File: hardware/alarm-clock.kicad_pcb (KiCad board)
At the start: 2 copper layers, 95.3 x 86.4 mm, 37 parts, among them CON1 BARREL_JACK, CON2 BARREL_JACK, IC1 ATMEGA328-P, Q1 Q_NPN_BCE, SW1 SWITCH_INV, SW2 SW_PUSH, SW3 SW_PUSH, U1 LM7805CT, U2 DS1307, U3 4Dig7Seg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

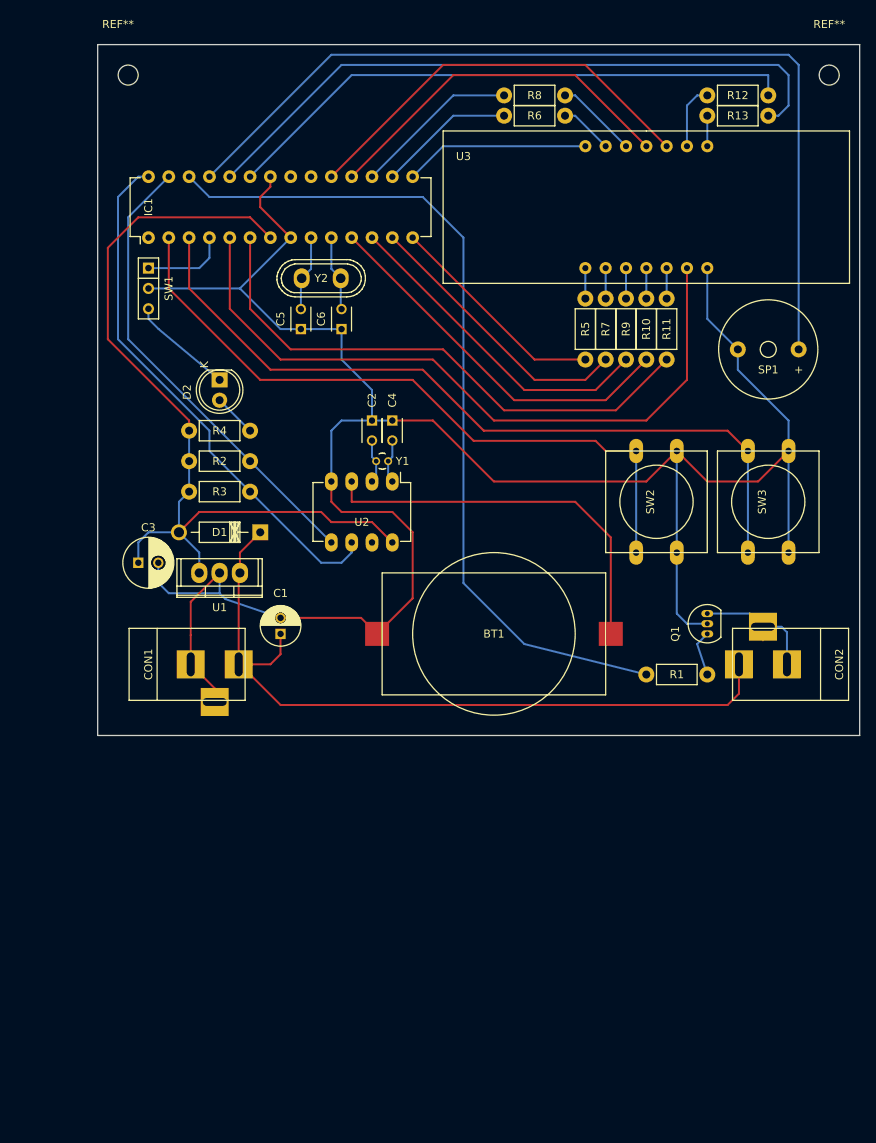
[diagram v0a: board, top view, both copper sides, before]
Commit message: Updated schematic w/ SMD and working buzzer
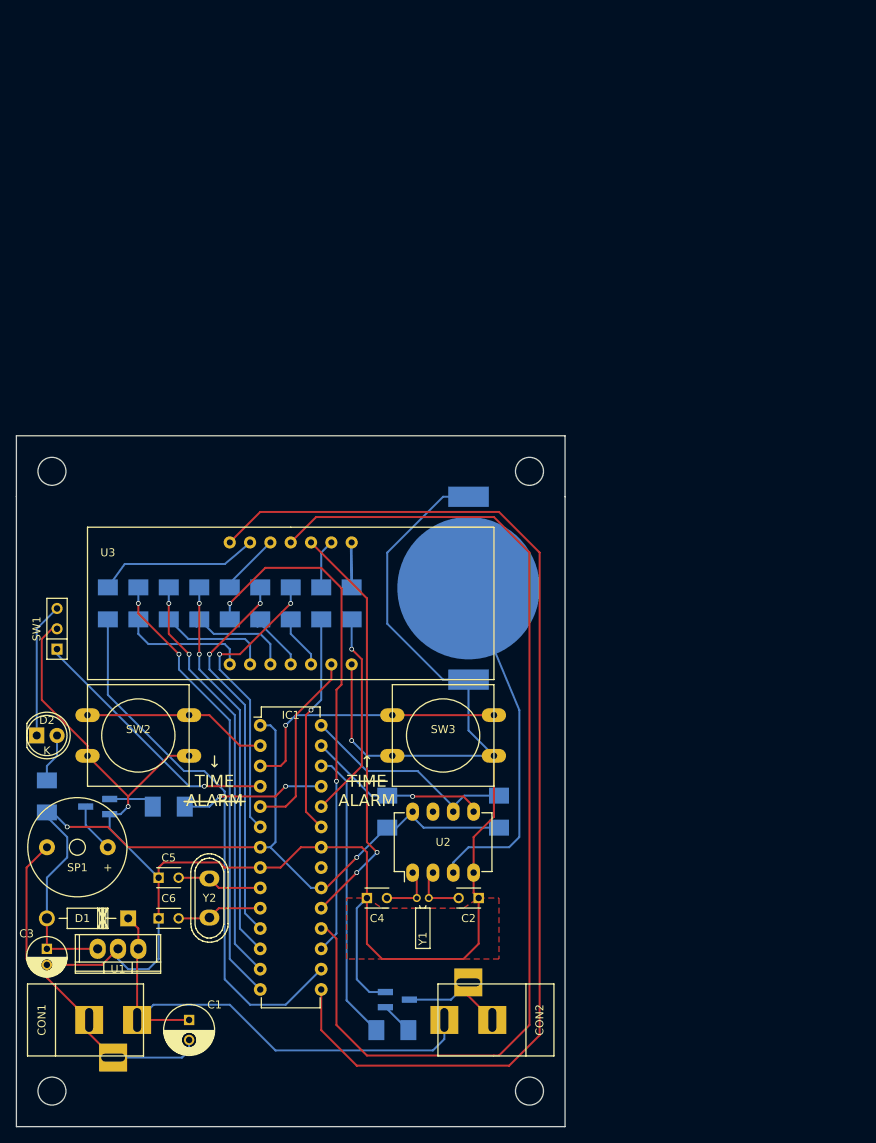
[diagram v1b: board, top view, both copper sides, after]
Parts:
- removed REF** (x2): MountingHole_2.5mm, Mounting_Holes:MountingHole_2.5mm
- added ?: MountingHole_3.5mm, Mounting_Holes:MountingHole_3.5mm, F.Cu at (118.7, 166.4)
- added ?: MountingHole_3.5mm, Mounting_Holes:MountingHole_3.5mm, F.Cu at (178.4, 88.9)
- added ?: MountingHole_3.5mm, Mounting_Holes:MountingHole_3.5mm, F.Cu at (118.7, 88.9)
- added ?: MountingHole_3.5mm, Mounting_Holes:MountingHole_3.5mm, F.Cu at (178.4, 166.4)
- added Q2: Q_NPN_BCE, TO_SOT_Packages_SMD:SOT-23_Handsoldering, B.Cu at (124.5, 130.8)
- added R14: 2.2k, Resistors_SMD:R_1210_HandSoldering, B.Cu at (156.2, 105.4)
- BT1: footprint custom:CR2032 -> custom:bat_holder_20mm_smd; moved to B.Cu
- C1: footprint Capacitors_ThroughHole:C_Radial_D5_L11_P2 -> Capacitors_ThroughHole:C_Radial_D6.3_L11.2_P2.5
- C3: footprint Capacitors_ThroughHole:C_Radial_D6.3_L11.2_P2.5 -> Capacitors_ThroughHole:C_Radial_D5_L11_P2
- Q1: footprint TO_SOT_Packages_THT:TO-92_Inline_Narrow_Oval -> TO_SOT_Packages_SMD:SOT-23_Handsoldering; moved to B.Cu
- R1, R10, R11, R12, R13, R3, R6, R7, R8, R9: footprint Resistors_ThroughHole:Resistor_Horizontal_RM7mm -> Resistors_SMD:R_1210_HandSoldering; moved to B.Cu
- R2: value 2.2k -> 3.3k; footprint Resistors_ThroughHole:Resistor_Horizontal_RM7mm -> Resistors_SMD:R_1210_HandSoldering; moved to B.Cu
- R4: value 270 -> 2.2k; footprint Resistors_ThroughHole:Resistor_Horizontal_RM7mm -> Resistors_SMD:R_1210_HandSoldering; moved to B.Cu
- R5: value 2.2k -> 270; footprint Resistors_ThroughHole:Resistor_Horizontal_RM7mm -> Resistors_SMD:R_1210_HandSoldering; moved to B.Cu
- Y1: footprint Crystals:Crystal_Round_Vertical_2mm -> Crystals:Crystal_Round_Horizontal_2mm
- moved SP1 106.4 mm to (121.9, 135.9)
- moved R5 91.7 mm to (118.1, 129.5), turned to 90 degrees
- moved R12 87.2 mm to (148.6, 105.4), turned to 90 degrees
- moved R13 82.7 mm to (152.4, 105.4), turned to 90 degrees
- moved Y2 78.7 mm to (138.4, 142.2), turned to 90 degrees
- moved C6 77.1 mm to (132.1, 144.8), turned to 0 degrees
- moved R6 76.2 mm to (129.5, 105.4), turned to 90 degrees
- moved R8 76.1 mm to (133.3, 105.4), turned to 90 degrees
- moved R7 73.0 mm to (125.7, 105.4), turned to 90 degrees
- moved SW2 71.1 mm to (129.5, 121.9), turned to 0 degrees
- moved C5 70.8 mm to (132.1, 139.7), turned to 0 degrees
- moved R10 67.6 mm to (137.2, 105.4), turned to 90 degrees
- moved U3 66.6 mm to (148.6, 105.4)
- moved R11 63.5 mm to (144.8, 105.4), turned to 90 degrees
- moved IC1 62.5 mm to (144.8, 120.7), turned to 0 degrees
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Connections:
- IC1 pad 1: (no net) -> +5V
- IC1 pad 20: (no net) -> +5V
- R10 pad 2: PD5 -> PD6
- R11 pad 2: PD4 -> PD5
- R12 pad 1: PC0 -> Net-(R12-Pad1)
- R12 pad 2: Net-(R12-Pad2) -> PD4
- R13 pad 1: PC1 -> PC0
- R2 pad 1: +5V -> PC2
- R2 pad 2: PC4 -> Net-(Q2-Pad1)
- R3 pad 2: PC5 -> PC4
- R4 pad 2: Net-(D2-Pad2) -> PC5
- R5 pad 1: Net-(R5-Pad1) -> +5V
- R5 pad 2: PB0 -> Net-(D2-Pad2)
- R6 pad 1: PB2 -> Net-(R6-Pad1)
- R6 pad 2: Net-(R6-Pad2) -> PB0
- R7 pad 1: Net-(R7-Pad1) -> PB2
- R7 pad 2: PD7 -> Net-(R7-Pad2)
- R8 pad 1: PB3 -> Net-(R8-Pad1)
- R8 pad 2: Net-(R8-Pad2) -> PD7
- R9 pad 1: Net-(R9-Pad1) -> PB3
- R9 pad 2: PD6 -> Net-(R9-Pad2)
- SP1 pad 1: PC2 -> Net-(Q2-Pad3)
- U3 pad 1: Net-(R5-Pad1) -> Net-(R6-Pad1)
- U3 pad 12: Net-(R8-Pad2) -> Net-(R9-Pad2)
- U3 pad 13: Net-(R6-Pad2) -> Net-(R7-Pad2)
- U3 pad 2: Net-(R7-Pad1) -> Net-(R8-Pad1)
- U3 pad 3: Net-(R9-Pad1) -> Net-(R10-Pad1)
- U3 pad 4: Net-(R10-Pad1) -> Net-(R11-Pad1)
- U3 pad 5: Net-(R11-Pad1) -> Net-(R12-Pad1)
- U3 pad 8: Net-(R13-Pad2) -> Net-(R14-Pad2)
- U3 pad 9: Net-(R12-Pad2) -> Net-(R13-Pad2)
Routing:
- net PB1: track 23.2 -> 138.5 mm
- net PC2: track 116.1 -> 18.1 mm, vias 0 -> 2
- net PB4: track 45.8 -> 132.6 mm
- net PC3: track 107.1 -> 37.3 mm
- net PD3: track 87.9 -> 23.3 mm
- net PD1: track 97.3 -> 34.4 mm, vias 0 -> 1
- net PD0: track 85.9 -> 23.2 mm
- net PC1: track 83.0 -> 26.0 mm, vias 0 -> 1
- net PB2: track 17.1 -> 67.7 mm
- net PB3: track 20.7 -> 65.6 mm, vias 0 -> 2
- net PC0: track 72.6 -> 29.0 mm, vias 0 -> 1
- net PC5: track 66.7 -> 28.3 mm
- net PC4: track 58.3 -> 22.8 mm, vias 0 -> 1
- net VPP: track 96.3 -> 64.3 mm
- net PD4: track 68.9 -> 37.2 mm, vias 0 -> 2
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- added copper zone on F.Cu, net GND
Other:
- board size 95.3 x 86.4 mm -> 68.6 x 86.4 mm
- rule pad_to_mask_clearance: 0.2 -> 0
- board text added: "↑ TIME ALARM"
- board text added: "↓ TIME ALARM"
